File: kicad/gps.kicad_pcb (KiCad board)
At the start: 4 copper layers, 84.1 x 61.7 mm, 67 parts, among them J1 Bus_PCI_Express_x1, J2 USB_C_Receptacle_USB2.0_16P, J3 Conn_01x02, J4 USB_C_Receptacle_USB2.0_16P, Q1 IRLML6344, U2 W25Q128JVP, U3 MCP25625T-E/ML, U4 RP2040, U5 NEO-M9N, X1 ABM8-272-T3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

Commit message: Fix DRC Violations
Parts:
- C7: value 1uF -> 1u
- moved R2 0.12 mm to (140.0, 116.8)
- moved R12 0.07 mm to (164.8, 116.3)
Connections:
- U4 pad 6: /MISO -> unconnected-(U4-GPIO4-Pad6)
- U4 pad 7: CS -> unconnected-(U4-GPIO5-Pad7)
- U4 pad 8: SCK -> unconnected-(U4-GPIO6-Pad8)
- U4 pad 9: /MOSI -> unconnected-(U4-GPIO7-Pad9)
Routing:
- net GND: track 17.1 -> 22.8 mm
- net Net-(Q1-G): track 0.00 -> 1.49 mm
- net CANSTBY: track 45.9 -> 47.2 mm
- net CANINT: track 33.1 -> 33.9 mm

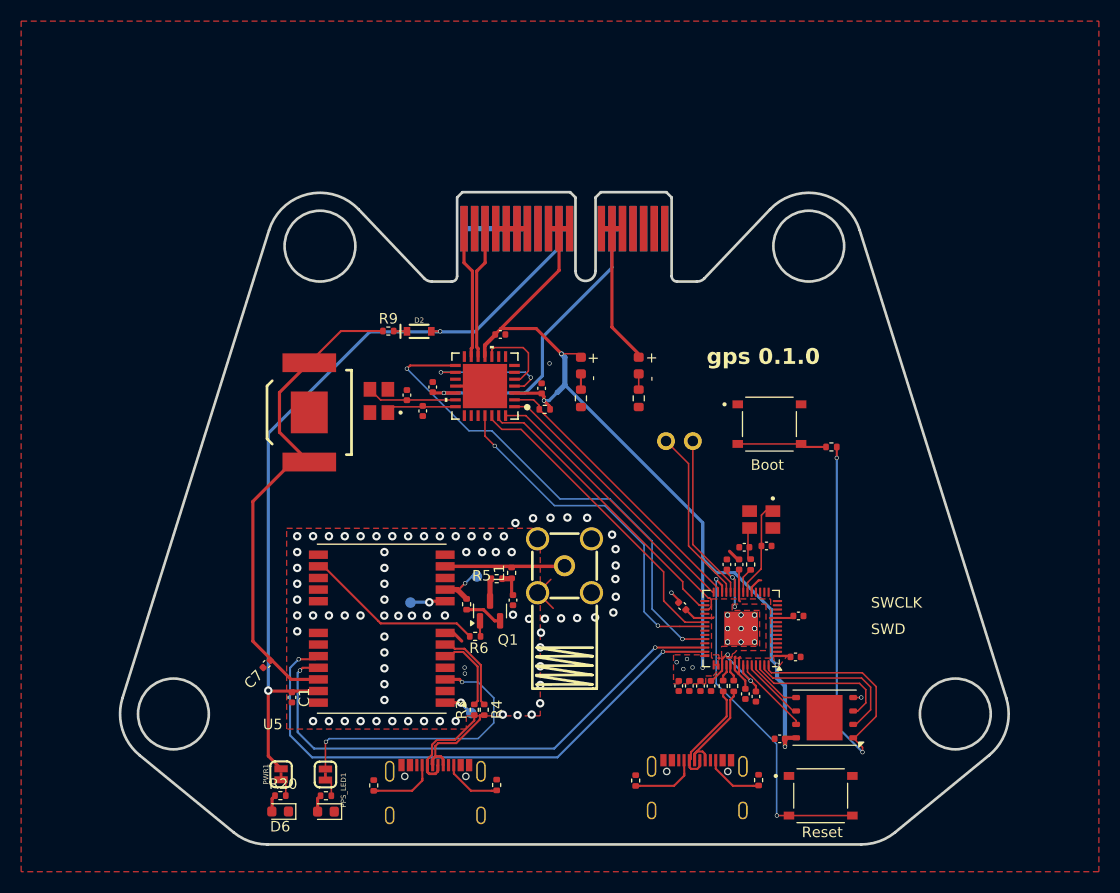
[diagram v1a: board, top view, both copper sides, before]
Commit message: Via Stitch
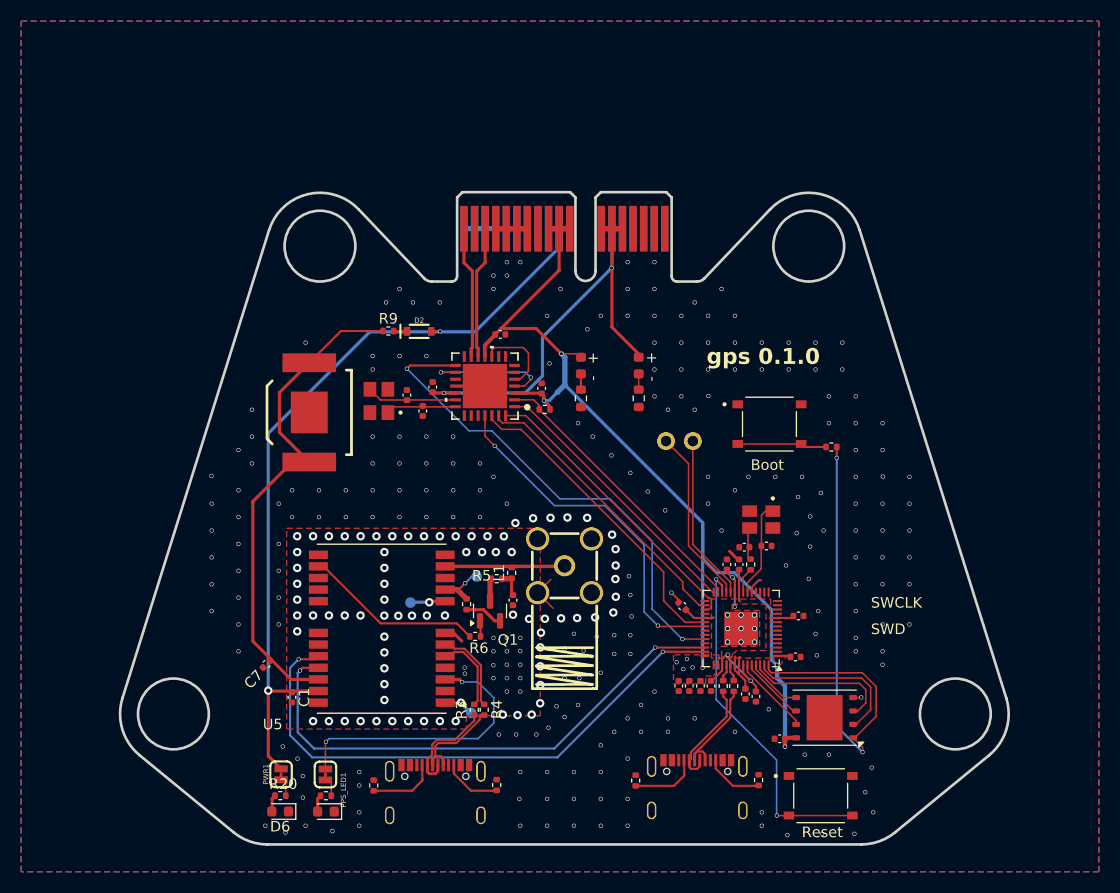
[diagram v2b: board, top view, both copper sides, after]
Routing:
- net +5V: track 45.4 -> 45.5 mm, vias 1 -> 2
- net GND: vias 91 -> 326
- added copper zone on B.Cu, net GND
- removed copper zone on In1.Cu, net GND

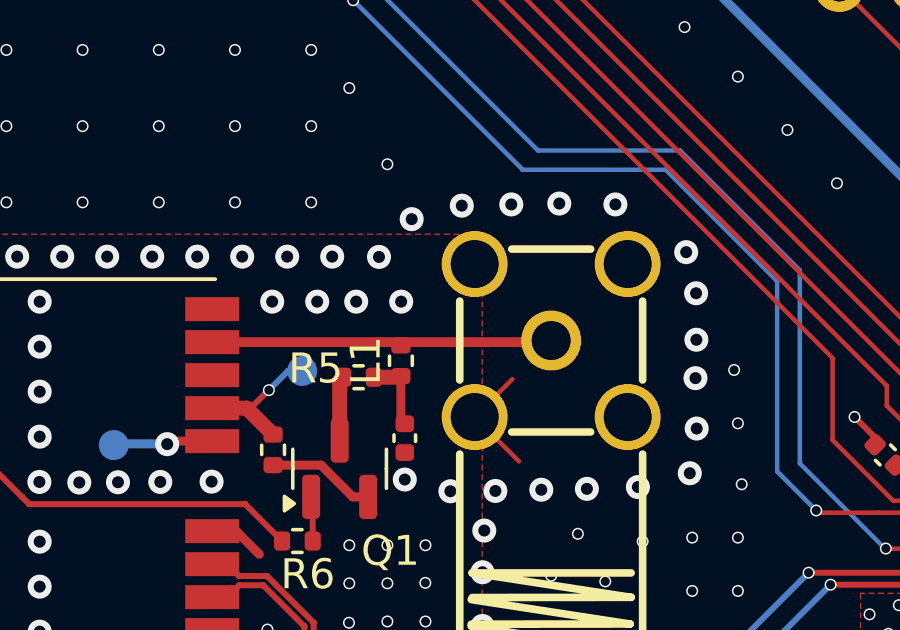
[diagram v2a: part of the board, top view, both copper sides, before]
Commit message: Add TVS Diode to footprint
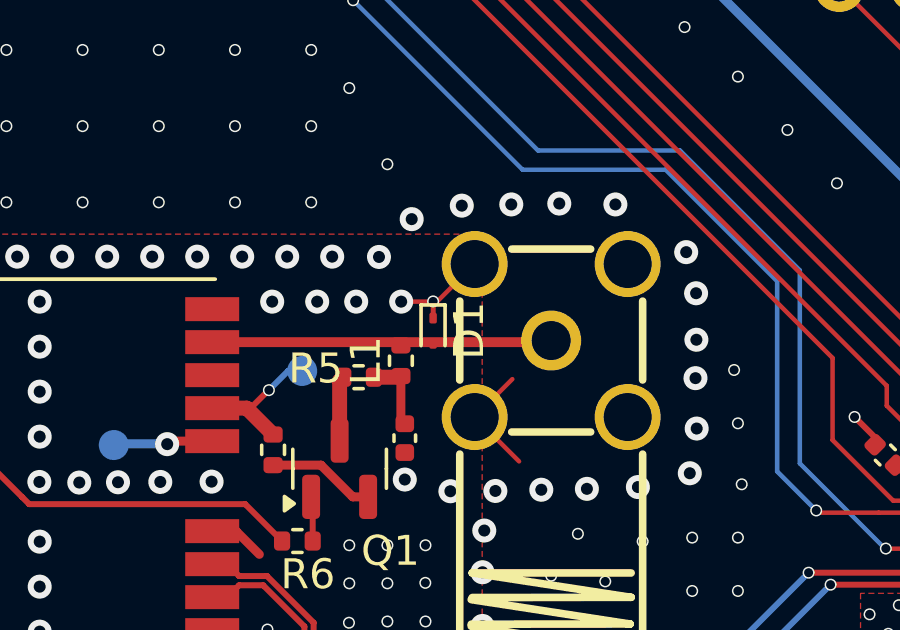
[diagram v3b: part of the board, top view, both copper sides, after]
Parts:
- added D1: PESD9R3.3ST5G, Diode_SMD:D_SOD-923, F.Cu at (142.5, 95.7)
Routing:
- net GND: track 22.8 -> 26.7 mm, vias 326 -> 327

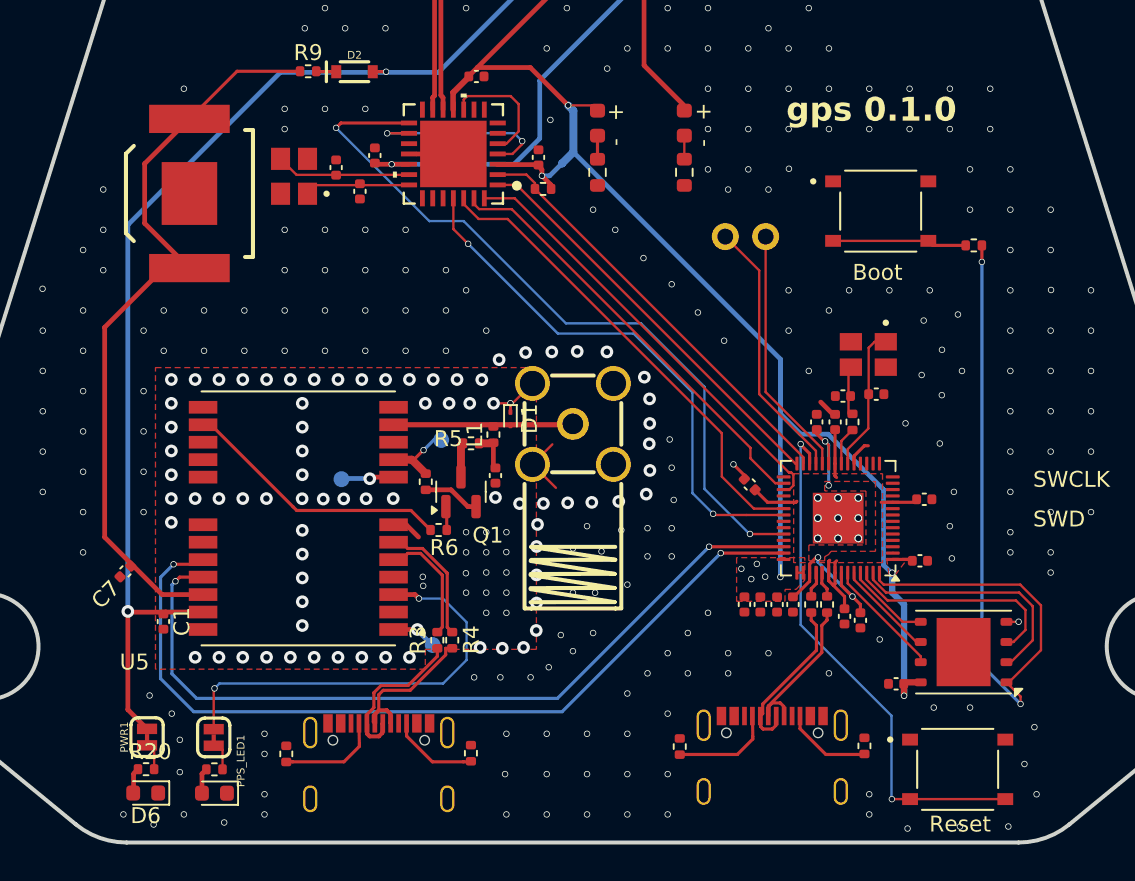
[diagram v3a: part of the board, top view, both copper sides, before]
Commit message: Update gate resistor value and apply general BOM improvements
- Changed gate resistor R6 from 10kΩ to 2.2kΩ to improve MOSFET switching speed while maintaining safe drive current for LNA_EN pin.
- Updated associated resistor part to a 0402 UNI-ROYAL 2.2kΩ variant with high stock from JLCPCB.
- Refined BOM fields for several components including RF connector (RF1) and battery holder (BAT1) to match R5 formatting.
- Ensured consistent metadata across all key parts: datasheets, LCSC part numbers, and manufacturer info.
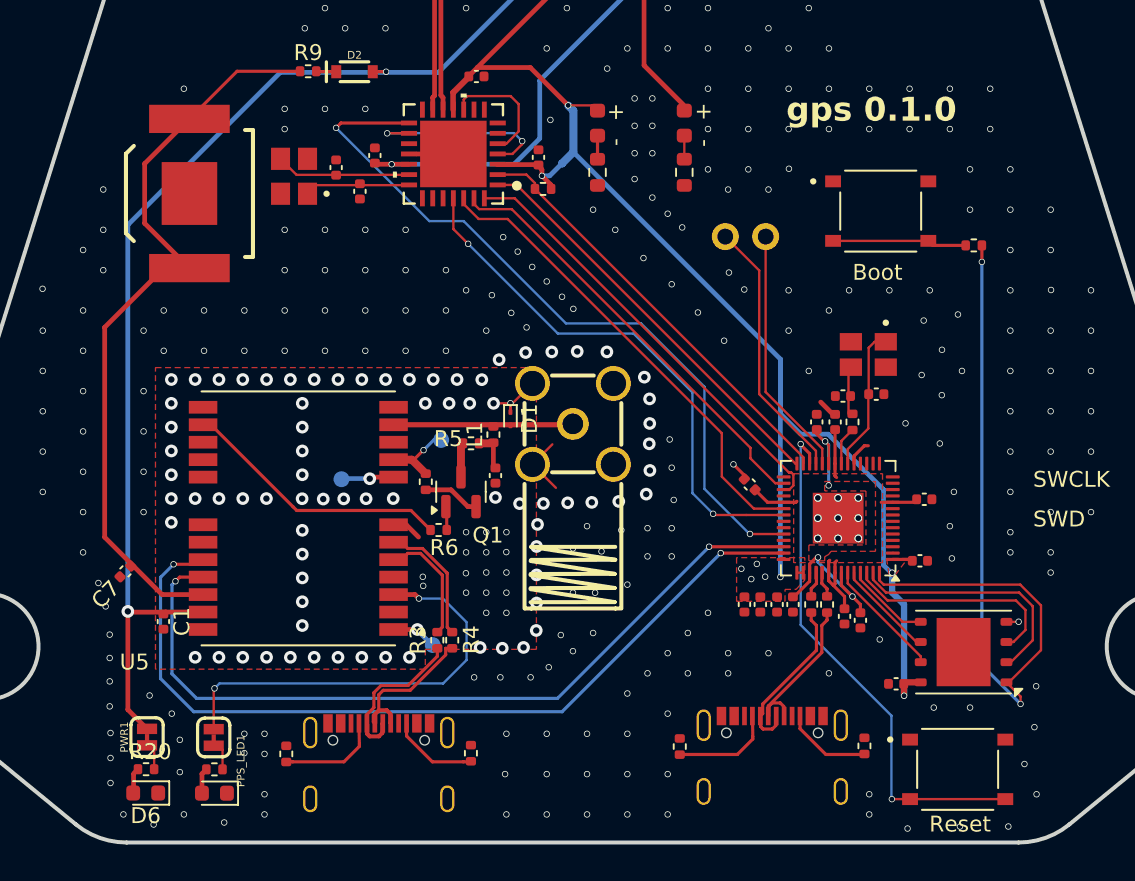
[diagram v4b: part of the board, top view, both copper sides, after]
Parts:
- R6: value 10k -> 2.2k
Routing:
- net GND: vias 327 -> 360

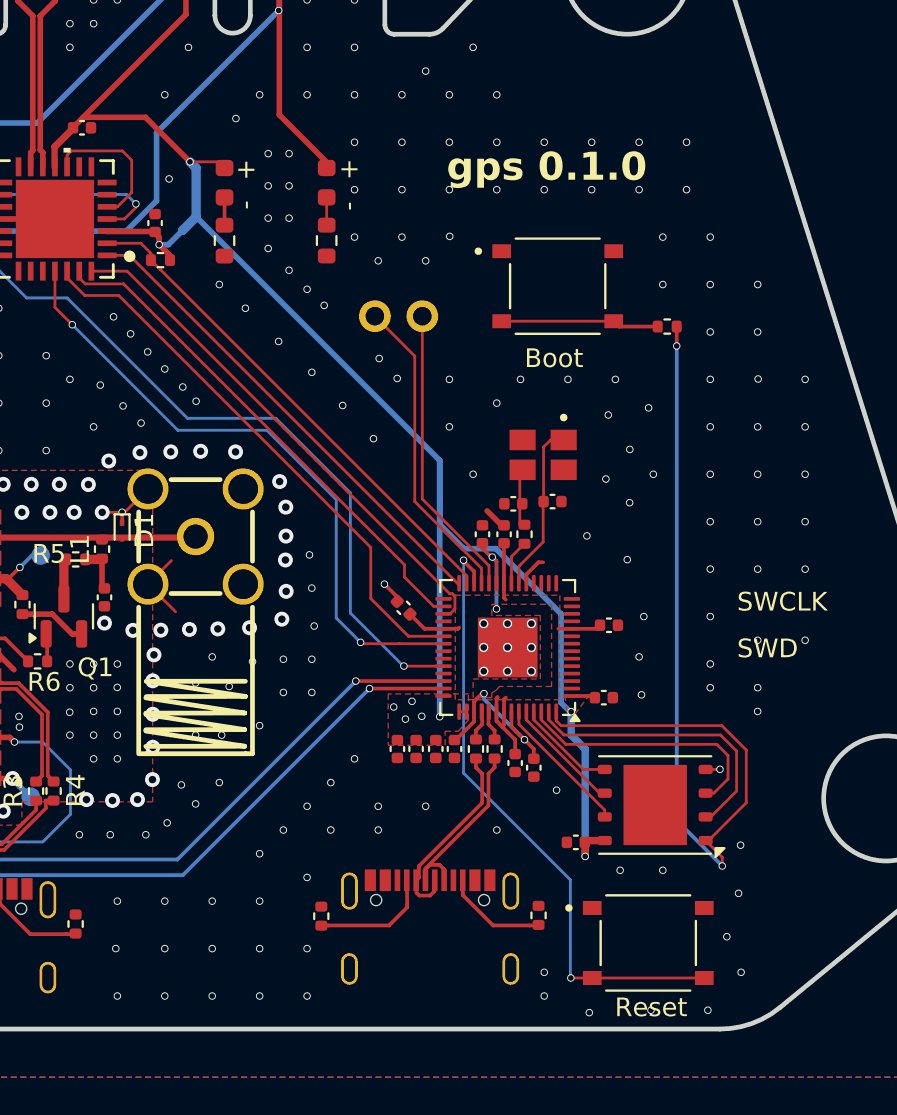
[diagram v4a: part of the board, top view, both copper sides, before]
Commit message: Update LED Positions
Move LEDs to the front of the board for 3.3V and 5V power
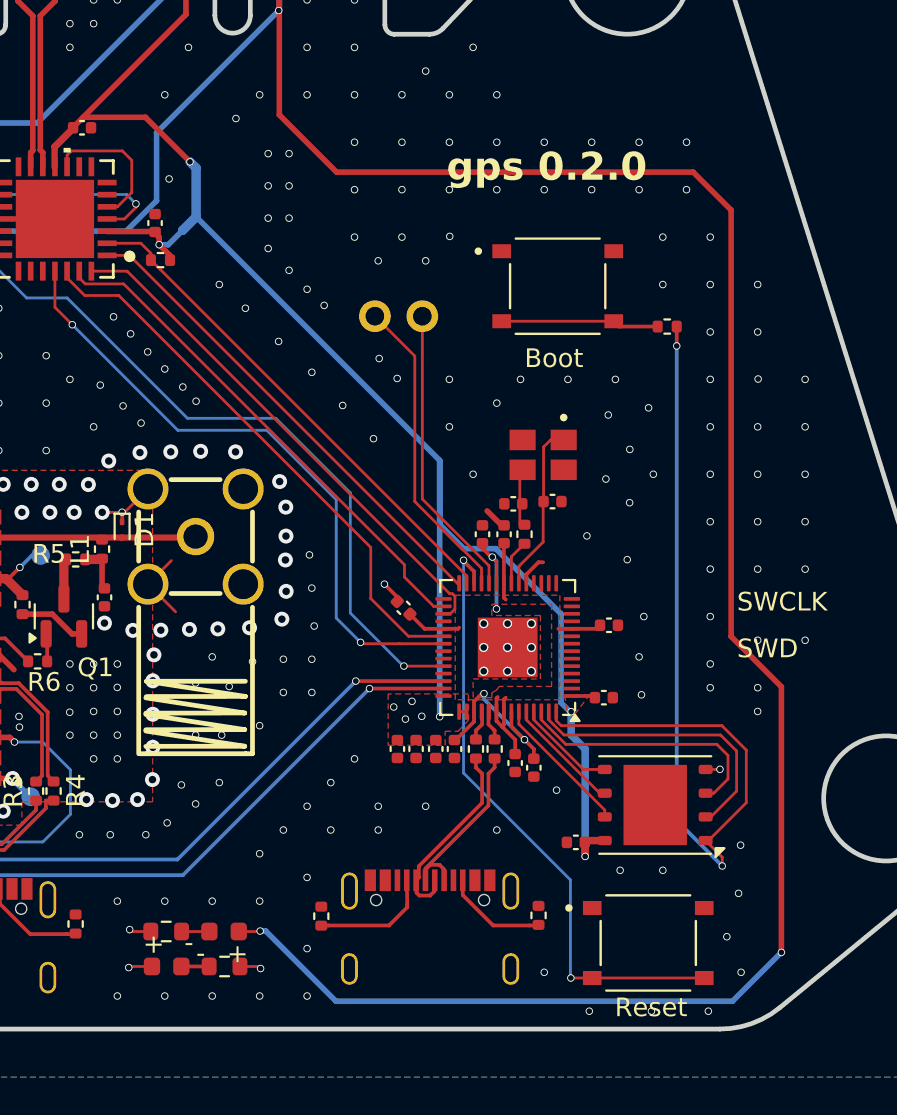
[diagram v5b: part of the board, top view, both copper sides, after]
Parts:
- moved D3 42.1 mm to (144.9, 119.1), turned to 180 degrees
- moved D4 40.5 mm to (148.0, 117.2), turned to 0 degrees
- moved R10 38.9 mm to (148.0, 119.1), turned to 0 degrees
- moved R13 38.0 mm to (144.9, 117.2), turned to 180 degrees
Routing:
- net +5V: track 45.5 -> 140.9 mm, vias 2 -> 4
- net GND: track 26.7 -> 29.0 mm, vias 360 -> 357
- net +3.3V: track 191.7 -> 190.9 mm, vias 11 -> 12
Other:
- board text added: "gps 0.2.0"
- board text removed: "gps 0.1.0"

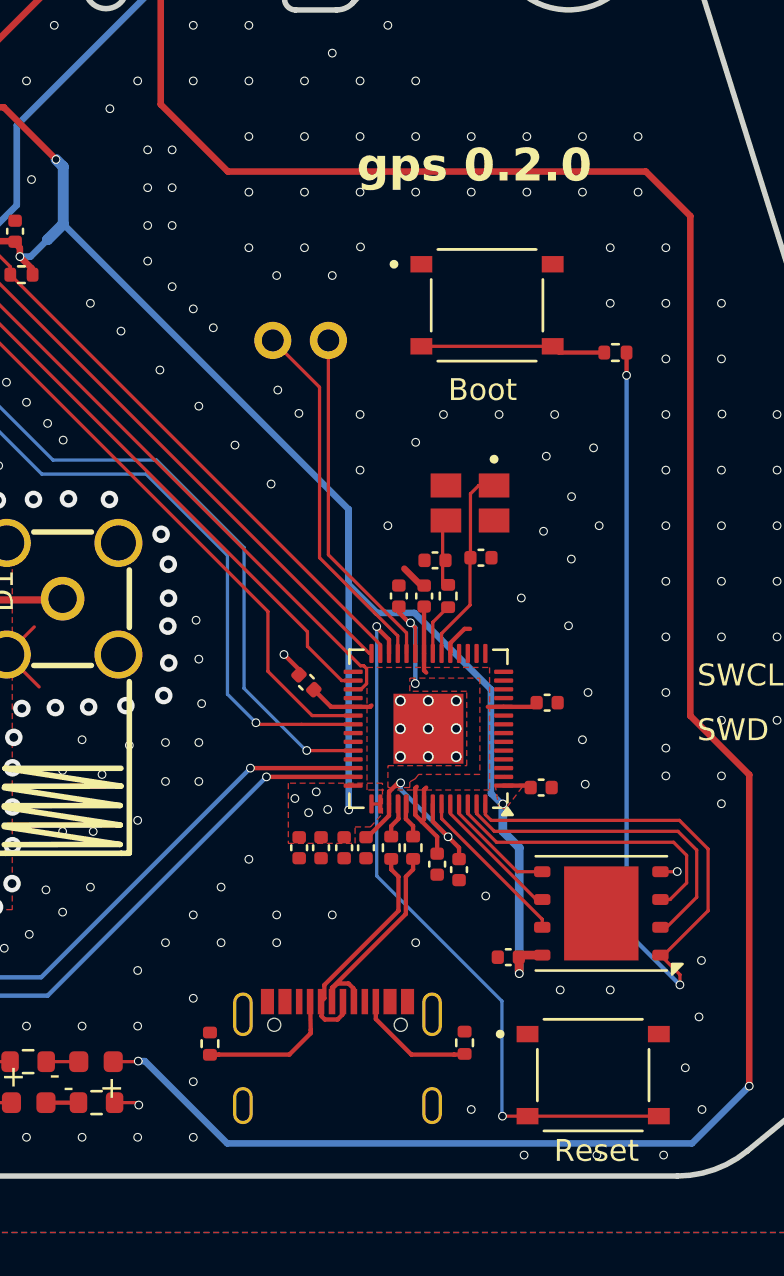
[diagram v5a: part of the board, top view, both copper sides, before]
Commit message: Move Gps Silkscreen to Front of Board
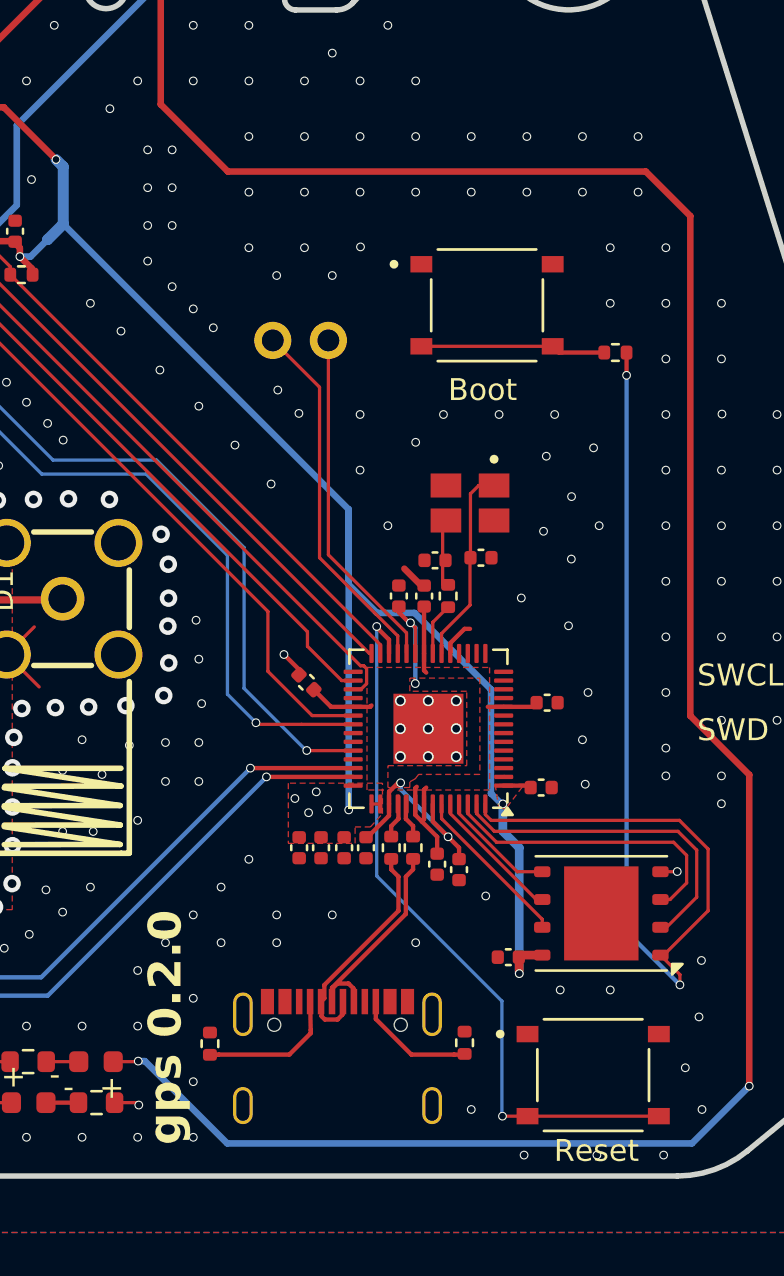
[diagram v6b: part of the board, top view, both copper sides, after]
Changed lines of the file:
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@@
 		(tags "resistor")
 		(property "Reference" "R10"
-			(at 0 -1.43 360)
+			(at 0 -1.43 0)
 			(layer "F.SilkS")
 			(hide yes)
@@
 		)
 		(property "Value" "1k"
-			(at 0 1.43 360)
+			(at 0 1.43 0)
 			(layer "F.Fab")
 			(effects
@@
 		)
 		(fp_text user "${REFERENCE}"
-			(at 0 0 360)
+			(at 0 0 0)
 			(layer "F.Fab")
 			(effects
@@
 		(tags "LED")
 		(property "Reference" "D3"
-			(at 0 -1.43 360)
+			(at 0 -1.43 0)
 			(layer "F.SilkS")
 			(hide yes)
@@
 		)
 		(property "Value" "LED"
-			(at -0.4572 1.4732 360)
+			(at -0.4572 1.4732 0)
 			(layer "F.Fab")
 			(effects
@@
 		)
 		(fp_text user "${REFERENCE}"
-			(at 0 0 360)
+			(at 0 0 0)
 			(layer "F.Fab")
 			(effects
@@
 		(tags "LED")
 		(property "Reference" "D4"
-			(at 0 -1.43 360)
+			(at 0 -1.43 0)
 			(layer "F.SilkS")
 			(hide yes)
@@
 		)
 		(property "Value" "LED"
-			(at 0 1.43 360)
+			(at 0 1.43 0)
 			(layer "F.Fab")
 			(effects
@@
 		)
 		(fp_text user "${REFERENCE}"
-			(at 0 0 360)
+			(at 0 0 0)
 			(layer "F.Fab")
 			(effects
@@
 		(tags "resistor")
 		(property "Reference" "R13"
-			(at 0 1.57 360)
+			(at 0 1.57 0)
 			(layer "F.SilkS")
 			(hide yes)
@@
 		)
 		(property "Value" "1k"
-			(at 0 1.43 360)
+			(at 0 1.43 0)
 			(layer "F.Fab")
 			(effects
@@
 		)
 		(fp_text user "${REFERENCE}"
-			(at 0 0 360)
+			(at 0 0 0)
 			(layer "F.Fab")
 			(effects
@@
 	)
 	(gr_text "gps 0.2.0"
-		(at 159.866 77.123 0)
+		(at 152 121 90)
 		(layer "F.SilkS")
 		(effects
